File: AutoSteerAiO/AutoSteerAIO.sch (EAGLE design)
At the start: 86 parts, among them K4 CB1A-P-12V, U1 VX7805-1000

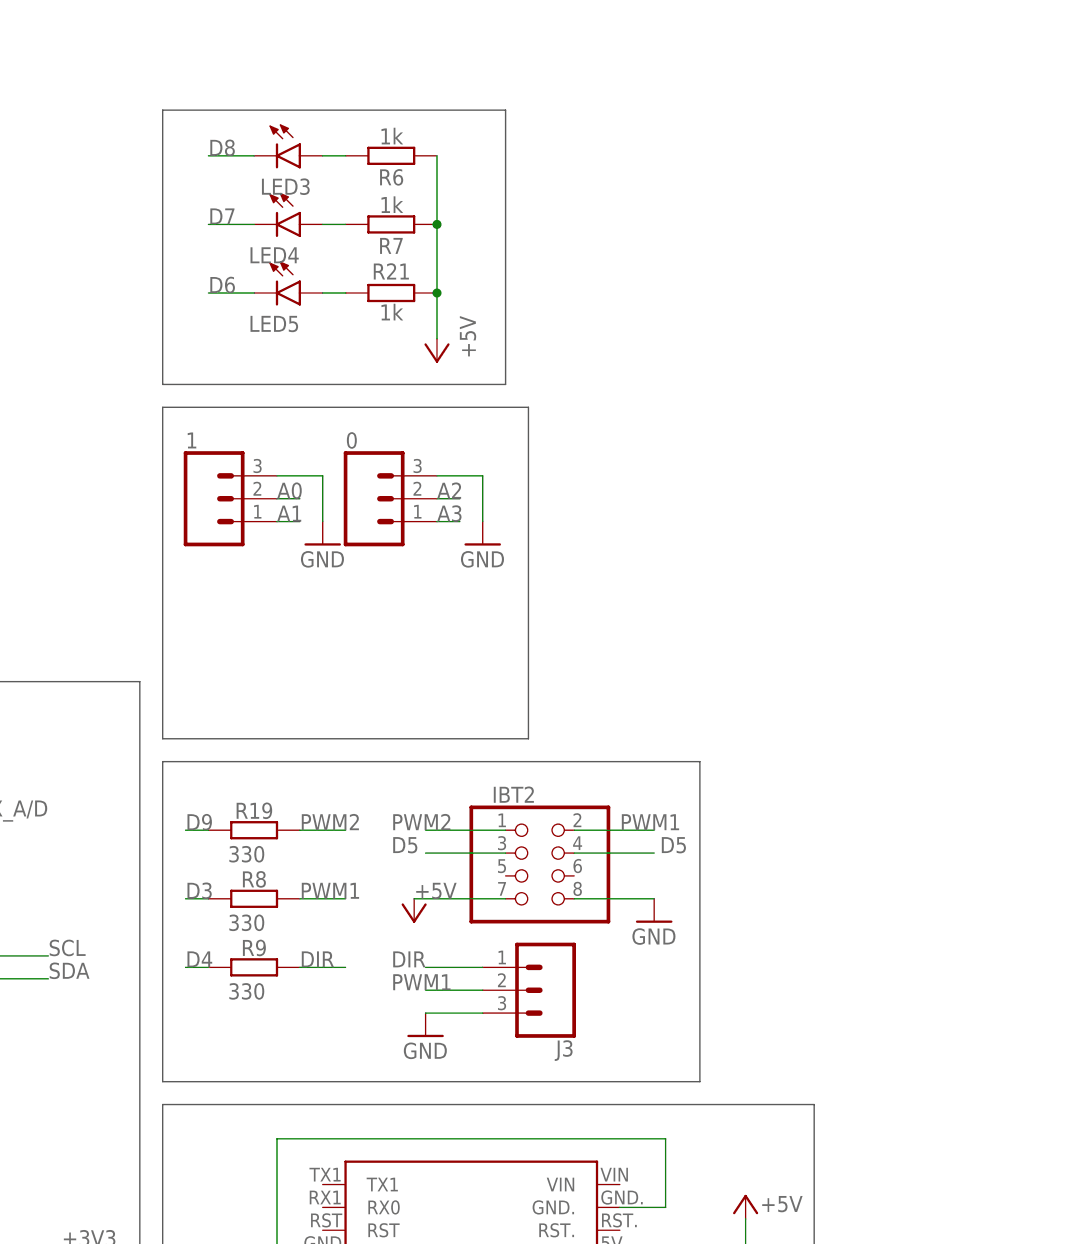
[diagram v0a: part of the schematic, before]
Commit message: Added selector for En IBT2, you can also use the new AutosteerPCBv2.ino sketch
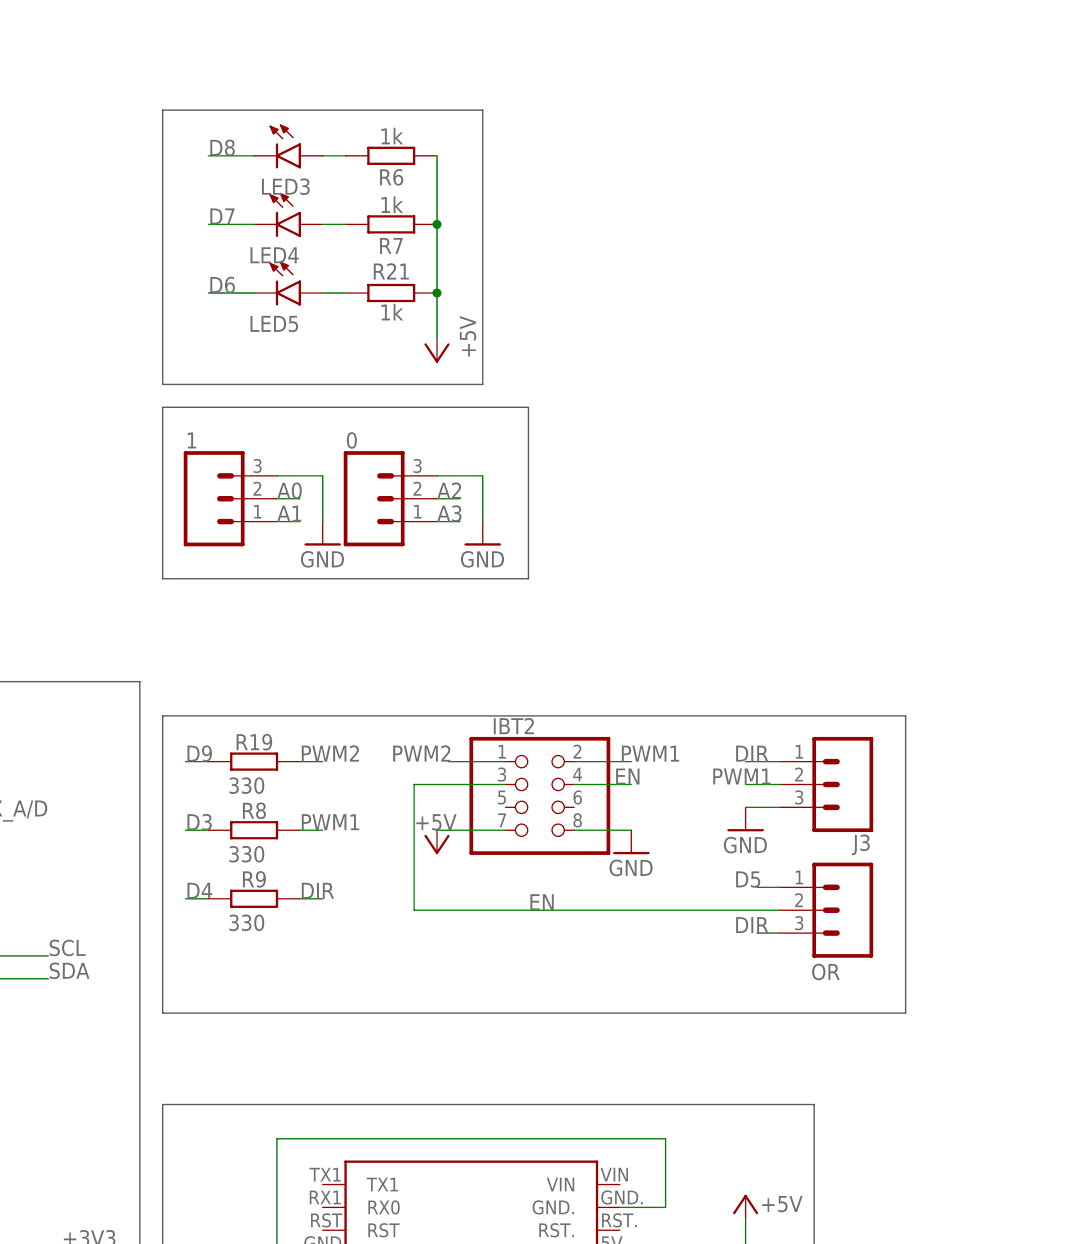
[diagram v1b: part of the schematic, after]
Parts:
- added OR: CONNECTOR 1x3 PINS, SparkFun-Connectors:CONN_03
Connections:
- new net EN: IBT2.3, IBT2.4, OR.2
- net D5: now also OR.1; no longer IBT2.3, IBT2.4
- net DIR: now also OR.3
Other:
- moved on the sheet: IBT2, J3, R19, R8, R9

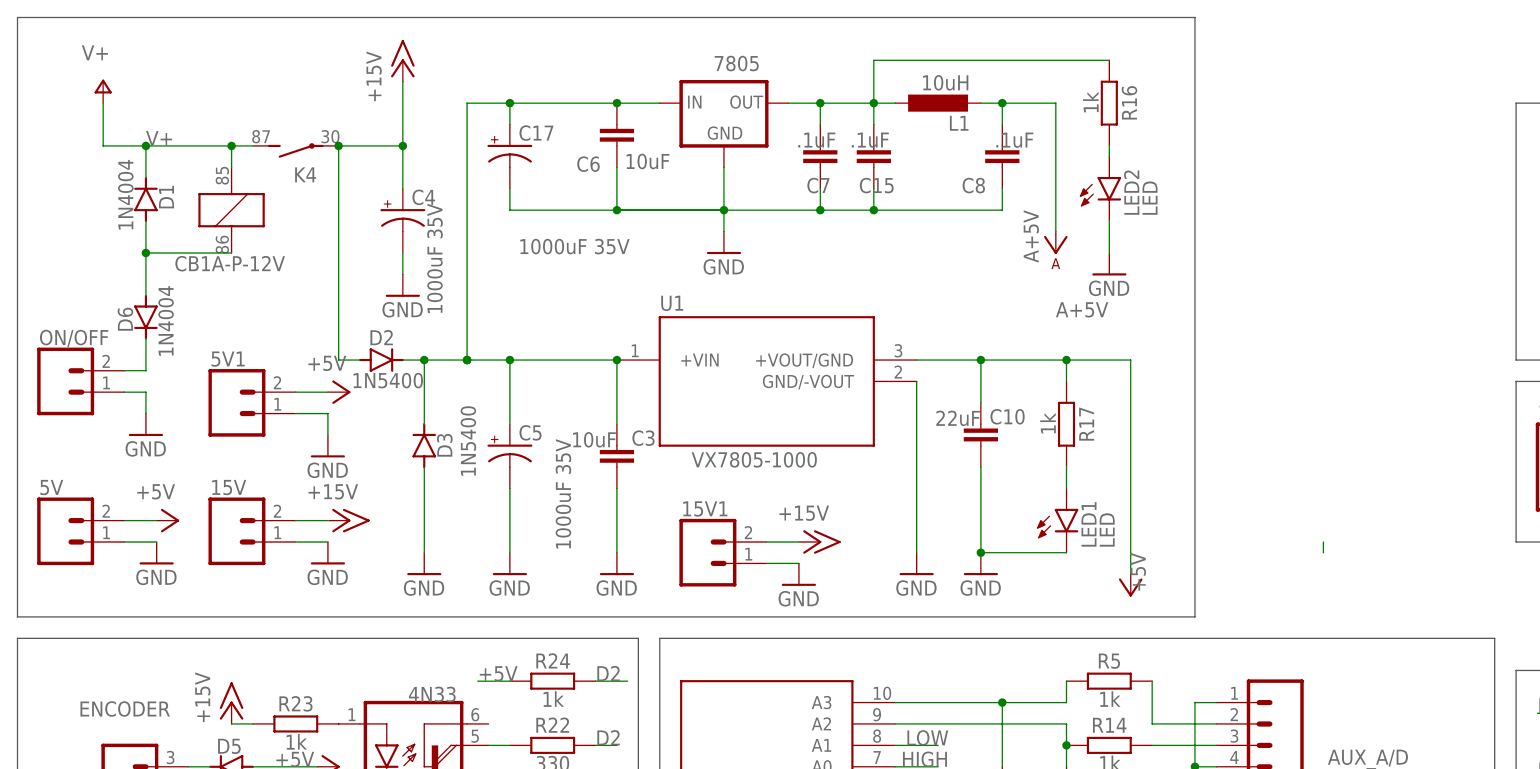
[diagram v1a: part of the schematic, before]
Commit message: Added one more 15V connector
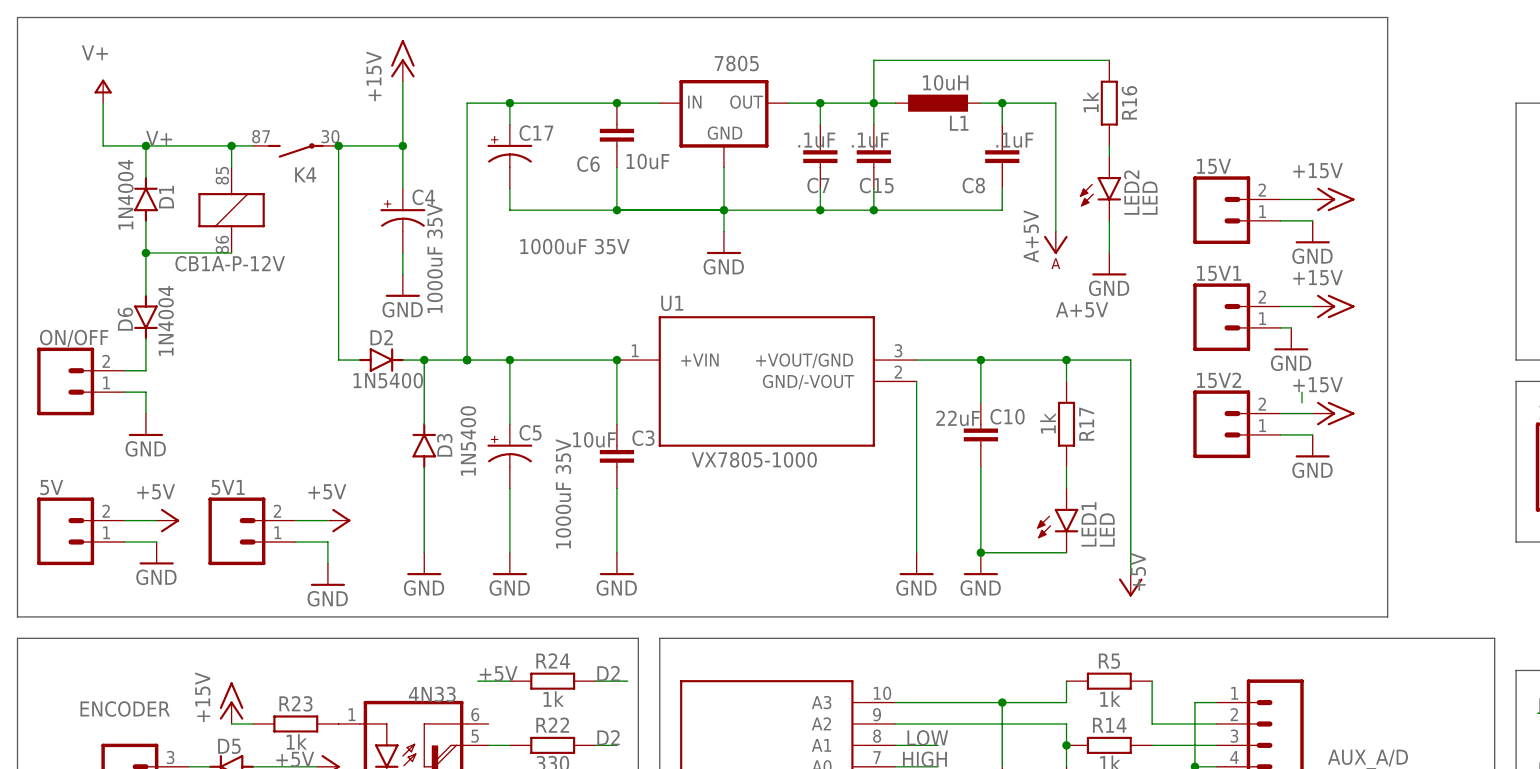
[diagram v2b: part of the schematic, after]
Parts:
- added 15V2: CONNECTOR 1x2 PINS, SparkFun-Connectors:CONN_02
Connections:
- net +15V: now also 15V2.2
- net GND: now also 15V2.1
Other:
- moved on the sheet: 15V, 15V1, 5V1
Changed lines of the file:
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@@
 <attribute name="OC_NEWARK" value="unknown"/>
 </part>
+<part name="15V2" library="SparkFun-Connectors" library_urn="urn:adsk.eagle:library:513" deviceset="CONN_02" device="" package3d_urn="urn:adsk.eagle:package:38039/1" value="CONNECTOR 1x2 PINS">
+<attribute name="MF" value=""/>
+<attribute name="MPN" value=""/>
+<attribute name="OC_NEWARK" value="unknown"/>
+</part>
+<part name="P+17" library="supply1" library_urn="urn:adsk.eagle:library:371" deviceset="+15V" device=""/>
+<part name="GND32" library="supply1" library_urn="urn:adsk.eagle:library:371" deviceset="GND" device=""/>
 </parts>
 <sheets>
@@
 <wire x1="157.48" y1="198.12" x2="58.42" y2="198.12" width="0.1524" layer="97"/>
 <wire x1="-17.78" y1="200.66" x2="-17.78" y2="271.78" width="0.1524" layer="97"/>
-<wire x1="121.92" y1="271.78" x2="-17.78" y2="271.78" width="0.1524" layer="97"/>
-<wire x1="121.92" y1="200.66" x2="121.92" y2="271.78" width="0.1524" layer="97"/>
-<wire x1="121.92" y1="200.66" x2="-17.78" y2="200.66" width="0.1524" layer="97"/>
+<wire x1="144.78" y1="271.78" x2="-17.78" y2="271.78" width="0.1524" layer="97"/>
+<wire x1="144.78" y1="200.66" x2="144.78" y2="271.78" width="0.1524" layer="97"/>
+<wire x1="144.78" y1="200.66" x2="-17.78" y2="200.66" width="0.1524" layer="97"/>
 <wire x1="160.02" y1="101.6" x2="160.02" y2="151.13" width="0.1524" layer="97"/>
 <wire x1="232.41" y1="101.6" x2="160.02" y2="101.6" width="0.1524" layer="97"/>
@@
 <attribute name="MPN" x="83.82" y="254" size="1.778" layer="96" display="off"/>
 </instance>
-<instance part="15V" gate="G$1" x="7.62" y="209.55" smashed="yes">
-<attribute name="NAME" x="5.08" y="215.138" size="1.778" layer="95" font="vector"/>
-<attribute name="OC_NEWARK" x="7.62" y="209.55" size="1.778" layer="96" display="off"/>
-<attribute name="MF" x="7.62" y="209.55" size="1.778" layer="96" display="off"/>
-<attribute name="MPN" x="7.62" y="209.55" size="1.778" layer="96" display="off"/>
-</instance>
-<instance part="P+4" gate="1" x="21.59" y="212.09" smashed="yes" rot="R270">
-<attribute name="VALUE" x="16.51" y="214.63" size="1.778" layer="96"/>
-</instance>
-<instance part="GND9" gate="1" x="19.05" y="207.01" smashed="yes">
-<attribute name="VALUE" x="16.51" y="204.47" size="1.778" layer="96"/>
+<instance part="15V" gate="G$1" x="124.46" y="247.65" smashed="yes">
+<attribute name="NAME" x="121.92" y="253.238" size="1.778" layer="95" font="vector"/>
+<attribute name="OC_NEWARK" x="124.46" y="247.65" size="1.778" layer="96" display="off"/>
+<attribute name="MF" x="124.46" y="247.65" size="1.778" layer="96" display="off"/>
+<attribute name="MPN" x="124.46" y="247.65" size="1.778" layer="96" display="off"/>
+</instance>
+<instance part="P+4" gate="1" x="138.43" y="250.19" smashed="yes" rot="R270">
+<attribute name="VALUE" x="133.35" y="252.73" size="1.778" layer="96"/>
+</instance>
+<instance part="GND9" gate="1" x="135.89" y="245.11" smashed="yes">
+<attribute name="VALUE" x="133.35" y="242.57" size="1.778" layer="96"/>
 </instance>
 <instance part="C17" gate="G$1" x="40.64" y="256.54" smashed="yes">
@@
 <attribute name="VALUE" x="54.864" y="245.491" size="1.778" layer="96" font="vector" rot="R180"/>
 </instance>
-<instance part="5V1" gate="G$1" x="7.62" y="224.79" smashed="yes">
-<attribute name="NAME" x="5.08" y="230.378" size="1.778" layer="95" font="vector"/>
-<attribute name="OC_NEWARK" x="7.62" y="224.79" size="1.778" layer="96" display="off"/>
-<attribute name="MF" x="7.62" y="224.79" size="1.778" layer="96" display="off"/>
-<attribute name="MPN" x="7.62" y="224.79" size="1.778" layer="96" display="off"/>
-</instance>
-<instance part="P+15" gate="1" x="21.59" y="227.33" smashed="yes" rot="R270">
-<attribute name="VALUE" x="16.51" y="229.87" size="1.778" layer="96"/>
-</instance>
-<instance part="GND20" gate="1" x="19.05" y="219.71" smashed="yes">
-<attribute name="VALUE" x="16.51" y="217.17" size="1.778" layer="96"/>
+<instance part="5V1" gate="G$1" x="7.62" y="209.55" smashed="yes">
+<attribute name="NAME" x="5.08" y="215.138" size="1.778" layer="95" font="vector"/>
+<attribute name="OC_NEWARK" x="7.62" y="209.55" size="1.778" layer="96" display="off"/>
+<attribute name="MF" x="7.62" y="209.55" size="1.778" layer="96" display="off"/>
+<attribute name="MPN" x="7.62" y="209.55" size="1.778" layer="96" display="off"/>
+</instance>
+<instance part="P+15" gate="1" x="21.59" y="212.09" smashed="yes" rot="R270">
+<attribute name="VALUE" x="16.51" y="214.63" size="1.778" layer="96"/>
+</instance>
+<instance part="GND20" gate="1" x="19.05" y="204.47" smashed="yes">
+<attribute name="VALUE" x="16.51" y="201.93" size="1.778" layer="96"/>
 </instance>
 <instance part="R20" gate="G$1" x="137.16" y="124.46" smashed="yes" rot="R180">
@@
 <attribute name="MPN" x="137.16" y="116.84" size="1.778" layer="96" display="off"/>
 </instance>
-<instance part="15V1" gate="G$1" x="63.5" y="207.01" smashed="yes">
-<attribute name="NAME" x="60.96" y="212.598" size="1.778" layer="95" font="vector"/>
-<attribute name="OC_NEWARK" x="63.5" y="207.01" size="1.778" layer="96" display="off"/>
-<attribute name="MF" x="63.5" y="207.01" size="1.778" layer="96" display="off"/>
-<attribute name="MPN" x="63.5" y="207.01" size="1.778" layer="96" display="off"/>
-</instance>
-<instance part="P+16" gate="1" x="77.47" y="209.55" smashed="yes" rot="R270">
-<attribute name="VALUE" x="72.39" y="212.09" size="1.778" layer="96"/>
-</instance>
-<instance part="GND34" gate="1" x="74.93" y="204.47" smashed="yes">
-<attribute name="VALUE" x="72.39" y="201.93" size="1.778" layer="96"/>
+<instance part="15V1" gate="G$1" x="124.46" y="234.95" smashed="yes">
+<attribute name="NAME" x="121.92" y="240.538" size="1.778" layer="95" font="vector"/>
+<attribute name="OC_NEWARK" x="124.46" y="234.95" size="1.778" layer="96" display="off"/>
+<attribute name="MF" x="124.46" y="234.95" size="1.778" layer="96" display="off"/>
+<attribute name="MPN" x="124.46" y="234.95" size="1.778" layer="96" display="off"/>
+</instance>
+<instance part="P+16" gate="1" x="138.43" y="237.49" smashed="yes" rot="R270">
+<attribute name="VALUE" x="133.35" y="240.03" size="1.778" layer="96"/>
+</instance>
+<instance part="GND34" gate="1" x="133.35" y="232.41" smashed="yes">
+<attribute name="VALUE" x="130.81" y="229.87" size="1.778" layer="96"/>
 </instance>
 <instance part="GND36" gate="1" x="129.54" y="109.22" smashed="yes">
@@
 <attribute name="MF" x="236.22" y="172.72" size="1.778" layer="96" rot="R180" display="off"/>
 <attribute name="MPN" x="236.22" y="172.72" size="1.778" layer="96" rot="R180" display="off"/>
+</instance>
+<instance part="15V2" gate="G$1" x="124.46" y="222.25" smashed="yes">
+<attribute name="NAME" x="121.92" y="227.838" size="1.778" layer="95" font="vector"/>
+<attribute name="OC_NEWARK" x="124.46" y="222.25" size="1.778" layer="96" display="off"/>
+<attribute name="MF" x="124.46" y="222.25" size="1.778" layer="96" display="off"/>
+<attribute name="MPN" x="124.46" y="222.25" size="1.778" layer="96" display="off"/>
+</instance>
+<instance part="P+17" gate="1" x="138.43" y="224.79" smashed="yes" rot="R270">
+<attribute name="VALUE" x="133.35" y="227.33" size="1.778" layer="96"/>
+</instance>
+<instance part="GND32" gate="1" x="135.89" y="219.71" smashed="yes">
+<attribute name="VALUE" x="133.35" y="217.17" size="1.778" layer="96"/>
 </instance>
 </instances>
@@
 <pinref part="5V1" gate="G$1" pin="2"/>
 <pinref part="P+15" gate="1" pin="+5V"/>
-<wire x1="15.24" y1="227.33" x2="19.05" y2="227.33" width="0.1524" layer="91"/>
+<wire x1="15.24" y1="212.09" x2="19.05" y2="212.09" width="0.1524" layer="91"/>
 </segment>
 </net>
@@
 <segment>
 <pinref part="15V" gate="G$1" pin="1"/>
-<wire x1="15.24" y1="209.55" x2="19.05" y2="209.55" width="0.1524" layer="91"/>
+<wire x1="132.08" y1="247.65" x2="135.89" y2="247.65" width="0.1524" layer="91"/>
 <pinref part="GND9" gate="1" pin="GND"/>
 </segment>
@@
 <pinref part="GND20" gate="1" pin="GND"/>
 <pinref part="5V1" gate="G$1" pin="1"/>
-<wire x1="19.05" y1="222.25" x2="19.05" y2="224.79" width="0.1524" layer="91"/>
-<wire x1="19.05" y1="224.79" x2="15.24" y2="224.79" width="0.1524" layer="91"/>
+<wire x1="19.05" y1="207.01" x2="19.05" y2="209.55" width="0.1524" layer="91"/>
+<wire x1="19.05" y1="209.55" x2="15.24" y2="209.55" width="0.1524" layer="91"/>
 </segment>
 <segment>
 <pinref part="15V1" gate="G$1" pin="1"/>
 <pinref part="GND34" gate="1" pin="GND"/>
-<wire x1="71.12" y1="207.01" x2="74.93" y2="207.01" width="0.1524" layer="91"/>
+<wire x1="132.08" y1="234.95" x2="133.35" y2="234.95" width="0.1524" layer="91"/>
 </segment>
 <segment>
@@
 <wire x1="127" y1="114.3" x2="129.54" y2="114.3" width="0.1524" layer="91"/>
 <wire x1="129.54" y1="114.3" x2="129.54" y2="111.76" width="0.1524" layer="91"/>
+</segment>
+<segment>
+<pinref part="15V2" gate="G$1" pin="1"/>
+<pinref part="GND32" gate="1" pin="GND"/>
+<wire x1="132.08" y1="222.25" x2="135.89" y2="222.25" width="0.1524" layer="91"/>
 </segment>
 </net>
@@
 <segment>
 <pinref part="15V" gate="G$1" pin="2"/>
-<wire x1="15.24" y1="212.09" x2="19.05" y2="212.09" width="0.1524" layer="91"/>
+<wire x1="132.08" y1="250.19" x2="135.89" y2="250.19" width="0.1524" layer="91"/>
 <pinref part="P+4" gate="1" pin="+15V"/>
 </segment>
@@
 <pinref part="15V1" gate="G$1" pin="2"/>
 <pinref part="P+16" gate="1" pin="+15V"/>
-<wire x1="71.12" y1="209.55" x2="74.93" y2="209.55" width="0.1524" layer="91"/>
+<wire x1="132.08" y1="237.49" x2="135.89" y2="237.49" width="0.1524" layer="91"/>
+</segment>
+<segment>
+<pinref part="15V2" gate="G$1" pin="2"/>
+<pinref part="P+17" gate="1" pin="+15V"/>
+<wire x1="132.08" y1="224.79" x2="135.89" y2="224.79" width="0.1524" layer="91"/>
 </segment>
 </net>
@@
 <net name="N$27" class="0">
 <segment>
-<wire x1="137.16" y1="209.55" x2="137.16" y2="208.28" width="0.1524" layer="91"/>
-</segment>
-</net>
+<wire x1="134.62" y1="227.33" x2="134.62" y2="226.06" width="0.1524" layer="91"/>
+</segment>
+</net>
